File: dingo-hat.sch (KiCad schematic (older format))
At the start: 50 parts, among them J1 6-13V, J14 NEOPIXEL, J15 MPU-9250, J16 4, J17 5, J18 6, J19 7, J2 Raspberry_Pi_2_3, J24 3mm_Mount, J25 3mm_Mount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

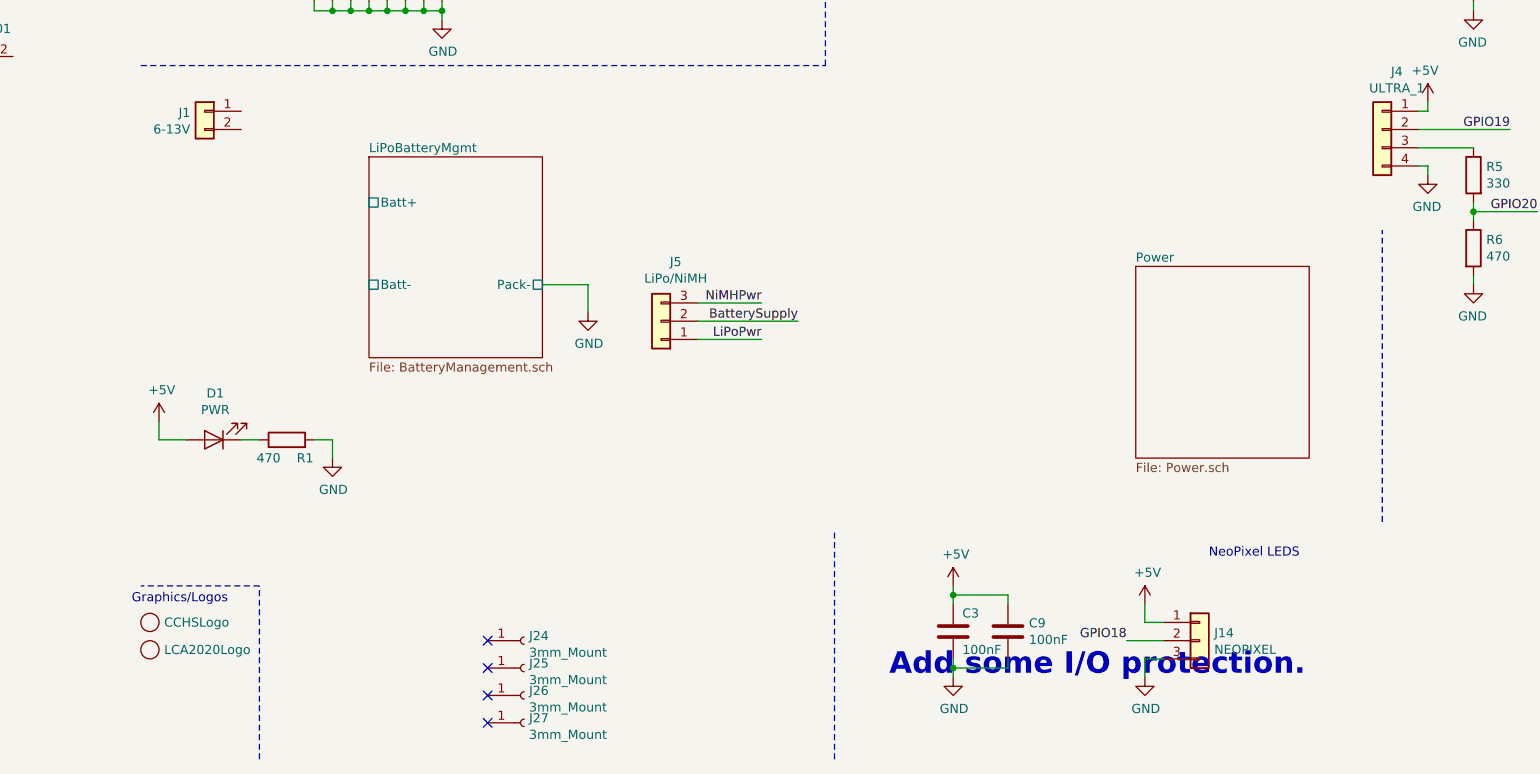
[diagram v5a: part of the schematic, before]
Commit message: Adding ADC for battery level.
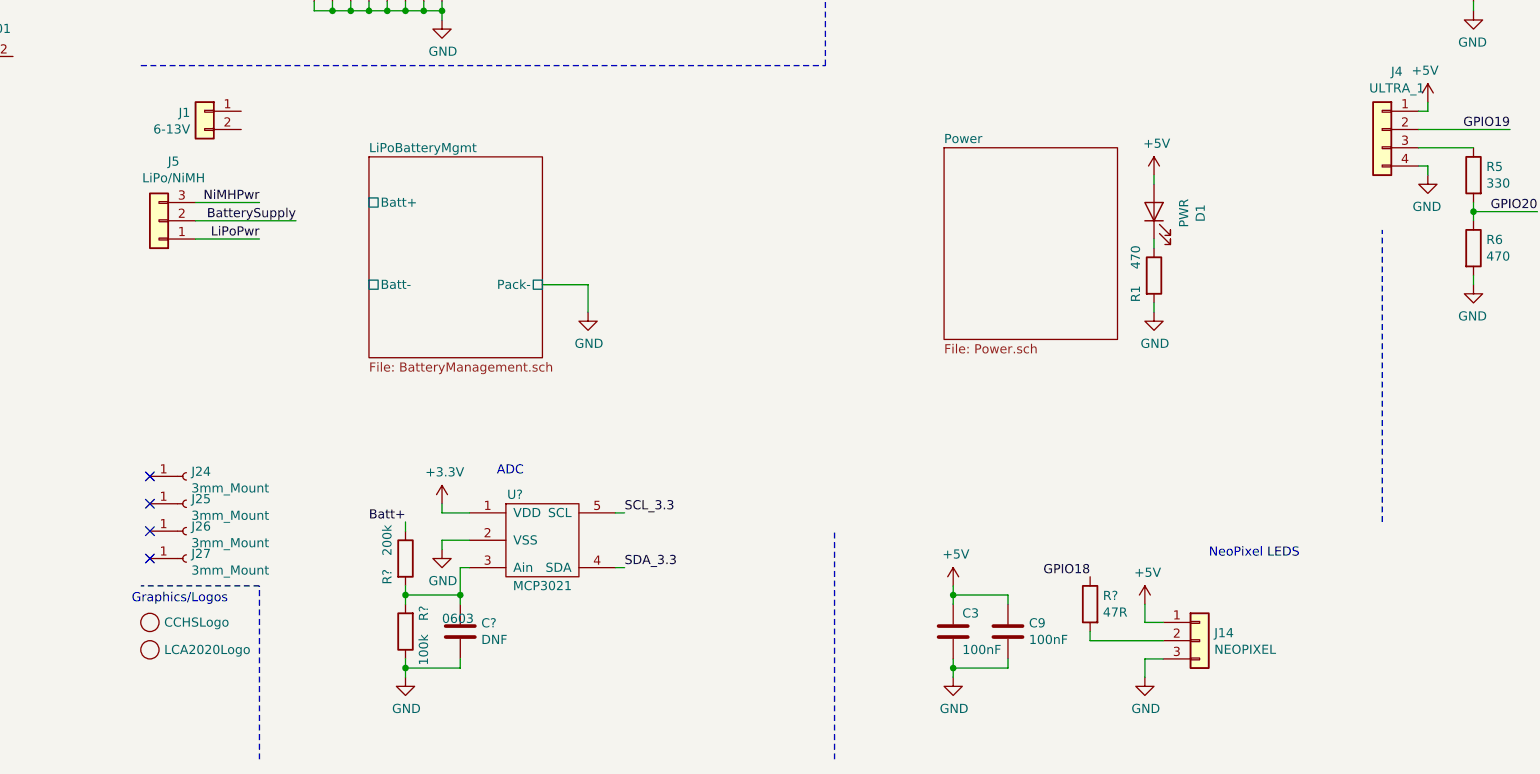
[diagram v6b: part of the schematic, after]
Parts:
- added C?: DNF, Capacitors_SMD:C_0603, symbol Device:C
- added R?: 100k, Resistors_SMD:R_0603, symbol Device:R
- added R?: 200k, Resistors_SMD:R_0603, symbol Device:R
- added R?: 47R, Resistors_SMD:R_0603, symbol Device:R
- added U?: MCP3021, TO_SOT_Packages_SMD:SOT-23-5, symbol dingo-hat:MCP3021
- R1, R3, R4, R5, R6, R7: footprint Resistor_SMD:R_0603_1608Metric_Pad1.05x0.95mm_HandSolder -> Resistors_SMD:R_0603
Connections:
- net +3V3: now also U?.1 (VDD)
- net GND: now also C?.2, R?.1, U?.2 (VSS)
- net GPIO18: now also R?.1; no longer J14.2 (Pin_2)
- net SCL_3.3: now also U?.5 (SCL)
- net SDA_3.3: now also U?.4 (SDA)
- new net: J14.2 (Pin_2), R?.2
- new net: C?.1, R?.2, R?.2, U?.3 (Ain)
- new net Batt+: R?.1
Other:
- note added: "ADC"
- note removed: "Add some I/O protection."
- moved on the sheet: D1, J24, J25, J26, J27, J5, R1

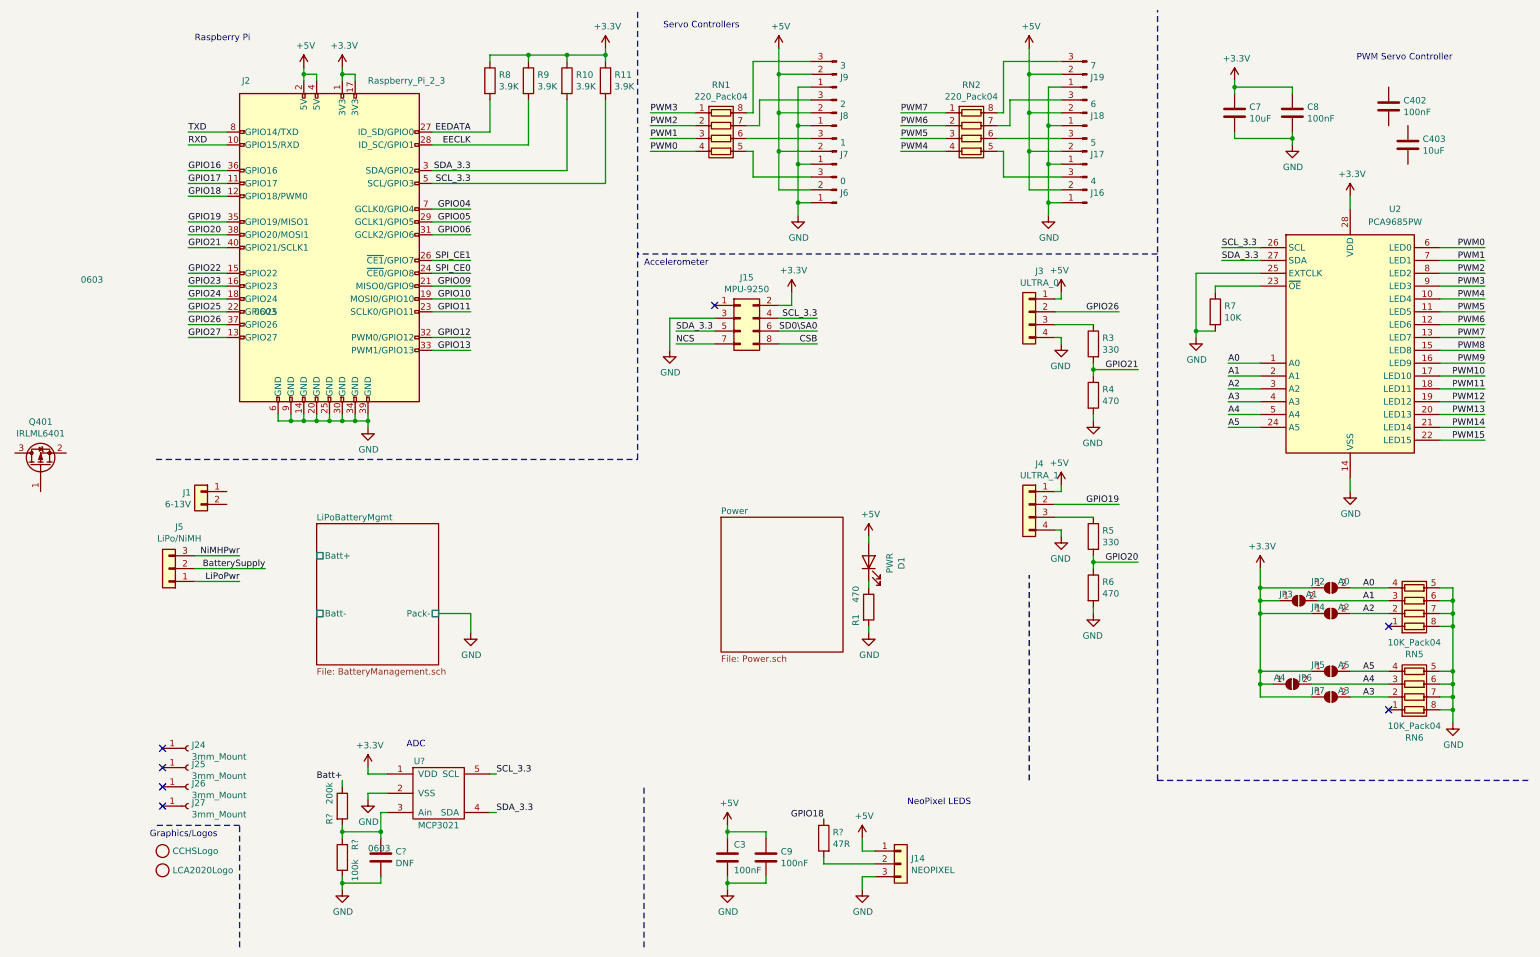
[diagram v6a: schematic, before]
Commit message: Getting rid of address block on PCA9685. We don't need that many options.
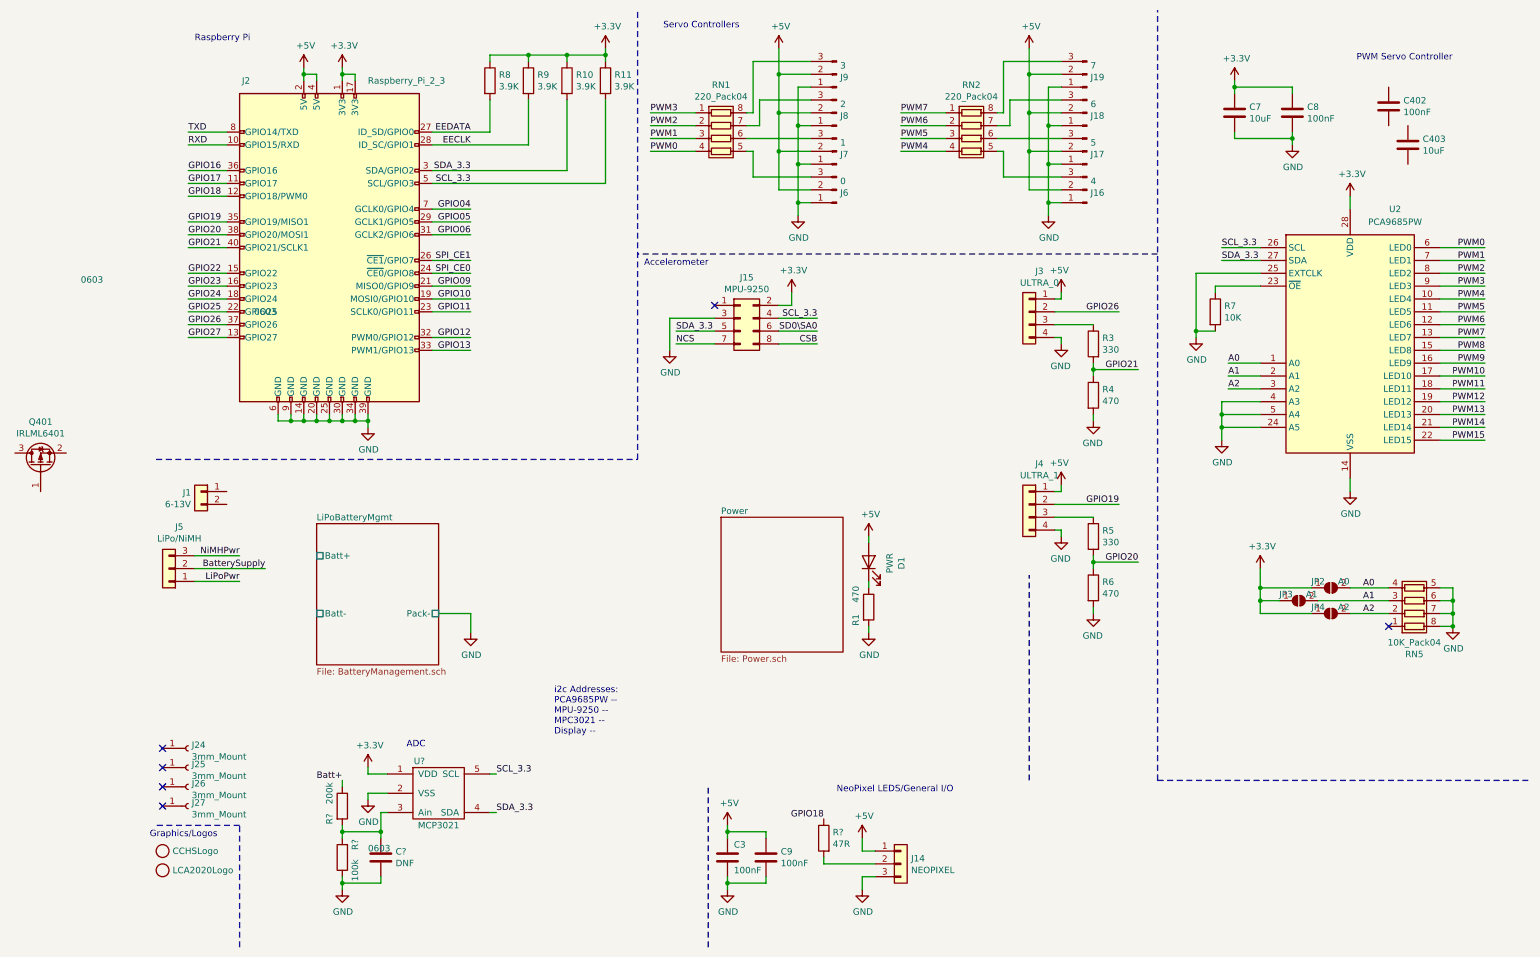
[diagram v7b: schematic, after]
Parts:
- removed JP5: A5, Jumper:SolderJumper-2_P1.3mm_Open_RoundedPad1.0x1.5mm, symbol Jumper:SolderJumper_2_Open
- removed JP6: A4, Jumper:SolderJumper-2_P1.3mm_Open_RoundedPad1.0x1.5mm, symbol Jumper:SolderJumper_2_Open
- removed JP7: A3, Jumper:SolderJumper-2_P1.3mm_Open_RoundedPad1.0x1.5mm, symbol Jumper:SolderJumper_2_Open
- removed RN6: 10K_Pack04, Resistor_SMD:R_Array_Convex_4x0603, symbol Device:R_Pack04
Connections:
- net A3 is gone; now on net GND: U2.4 (A3)
- net A4 is gone; now on net GND: U2.5 (A4)
- net A5 is gone; now on net GND: U2.24 (A5)
- no-connect marks 7 -> 6
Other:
- note added: "NeoPixel LEDS/General I/O"
- note added: "i2c Addresses:\nPCA9685PW --\nMPU-9250 --\nMPC3021 --\nDisplay --"
- note removed: "NeoPixel LEDS"
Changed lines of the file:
@@
 Text Label 8850 3450 0    50   ~ 0
 A2
-Wire Wire Line
-	9100 3550 8850 3550
-Text Label 8850 3550 0    50   ~ 0
-A3
-Wire Wire Line
-	9100 3650 8850 3650
-Text Label 8850 3650 0    50   ~ 0
-A4
-Wire Wire Line
-	9100 3750 8850 3750
-Text Label 8850 3750 0    50   ~ 0
-A5
 $Comp
 L Device:R R7
@@
 $EndComp
 $Comp
-L power:GND #PWR0107
-U 1 1 5C001B2D
-P 10600 6050
-F 0 "#PWR0107" H 10600 5800 50  0001 C CNN
-F 1 "GND" H 10605 5877 50  0000 C CNN
-F 2 "" H 10600 6050 50  0001 C CNN
-F 3 "" H 10600 6050 50  0001 C CNN
-	1    10600 6050
-	1    0    0    -1
-$EndComp
-$Comp
 L Jumper:SolderJumper_2_Open JP2
 U 1 1 5C001CDA
@@
 F 3 "~" H 9650 5200 50  0001 C CNN
 	1    9650 5200
-	1    0    0    -1
-$EndComp
-$Comp
-L Jumper:SolderJumper_2_Open JP5
-U 1 1 5C00261D
-P 9650 5650
-F 0 "JP5" H 9550 5700 50  0000 C CNN
-F 1 "A5" H 9750 5700 50  0000 C CNN
-F 2 "Jumper:SolderJumper-2_P1.3mm_Open_RoundedPad1.0x1.5mm" H 9650 5650 50  0001 C CNN
-F 3 "~" H 9650 5650 50  0001 C CNN
-	1    9650 5650
-	1    0    0    -1
-$EndComp
-$Comp
-L Jumper:SolderJumper_2_Open JP6
-U 1 1 5C002EE1
-P 9350 5750
-F 0 "JP6" H 9450 5800 50  0000 C CNN
-F 1 "A4" H 9250 5800 50  0000 C CNN
-F 2 "Jumper:SolderJumper-2_P1.3mm_Open_RoundedPad1.0x1.5mm" H 9350 5750 50  0001 C CNN
-F 3 "~" H 9350 5750 50  0001 C CNN
-	1    9350 5750
-	1    0    0    -1
-$EndComp
-$Comp
-L Jumper:SolderJumper_2_Open JP7
-U 1 1 5C002EE7
-P 9650 5850
-F 0 "JP7" H 9550 5900 50  0000 C CNN
-F 1 "A3" H 9750 5900 50  0000 C CNN
-F 2 "Jumper:SolderJumper-2_P1.3mm_Open_RoundedPad1.0x1.5mm" H 9650 5850 50  0001 C CNN
-F 3 "~" H 9650 5850 50  0001 C CNN
-	1    9650 5850
 	1    0    0    -1
 $EndComp
@@
 	6000 7250 6000 7350
 Wire Notes Line
-	4300 7800 4300 6550
-Text Notes 6350 6700 0    50   ~ 0
-NeoPixel LEDS
+	4800 7800 4800 6550
+Text Notes 5800 6600 0    50   ~ 0
+NeoPixel LEDS/General I/O
 Wire Notes Line
 	8300 2400 4250 2400
@@
 NoConn ~ 550  6700
 $Comp
-L Device:R_Pack04 RN6
-U 1 1 5C46C610
-P 10300 5750
-F 0 "RN6" V 9883 5750 50  0000 C CNN
-F 1 "10K_Pack04" V 9974 5750 50  0000 C CNN
-F 2 "Resistor_SMD:R_Array_Convex_4x0603" V 10575 5750 50  0001 C CNN
-F 3 "~" H 10300 5750 50  0001 C CNN
-F 4 "SMD" H 0   0   50  0001 C CNN "Package"
-	1    10300 5750
-	0    1    -1   0
-$EndComp
-$Comp
 L Device:R_Pack04 RN5
 U 1 1 5C4B78BC
@@
 	9100 4850 9100 5000
 Wire Wire Line
-	9100 5850 9500 5850
-Wire Wire Line
-	9200 5750 9100 5750
-Connection ~ 9100 5750
-Wire Wire Line
-	9100 5750 9100 5850
-Wire Wire Line
-	9500 5650 9100 5650
-Connection ~ 9100 5650
-Wire Wire Line
-	9100 5650 9100 5750
-Wire Wire Line
 	9100 5000 9500 5000
 Connection ~ 9100 5000
@@
 Wire Wire Line
 	9500 5200 9100 5200
-Connection ~ 9100 5200
-Wire Wire Line
-	9100 5200 9100 5650
-Wire Wire Line
-	9800 5650 10100 5650
-Wire Wire Line
-	9500 5750 10100 5750
-Wire Wire Line
-	9800 5850 10100 5850
 Wire Wire Line
 	10500 5000 10600 5000
@@
 	10600 5000 10600 5100
 Wire Wire Line
-	10500 5950 10600 5950
-Connection ~ 10600 5950
-Wire Wire Line
-	10600 5950 10600 6050
-Wire Wire Line
-	10600 5850 10500 5850
-Connection ~ 10600 5850
-Wire Wire Line
-	10600 5850 10600 5950
-Wire Wire Line
-	10500 5750 10600 5750
-Connection ~ 10600 5750
-Wire Wire Line
-	10600 5750 10600 5850
-Wire Wire Line
-	10500 5650 10600 5650
-Connection ~ 10600 5650
-Wire Wire Line
-	10600 5650 10600 5750
-Wire Wire Line
 	10500 5300 10600 5300
-Connection ~ 10600 5300
-Wire Wire Line
-	10600 5300 10600 5650
 Wire Wire Line
 	10500 5200 10600 5200
@@
 	9800 5200 10100 5200
 NoConn ~ 10100 5300
-NoConn ~ 10100 5950
 Text Label 9900 5000 0    50   ~ 0
 A0
@@
 Text Label 9900 5200 0    50   ~ 0
 A2
-Text Label 9900 5850 0    50   ~ 0
-A3
-Text Label 9900 5750 0    50   ~ 0
-A4
-Text Label 9900 5650 0    50   ~ 0
-A5
 $Comp
 L Device:C C9
@@
 Text Notes 2450 6250 0    50   ~ 0
 ADC
+Text Notes 3600 6150 0    50   ~ 0
+i2c Addresses:\nPCA9685PW --\nMPU-9250 --\nMPC3021 --\nDisplay --
+$Comp
+L power:GND #PWR?
+U 1 1 5E262FFC
+P 10600 5300
+F 0 "#PWR?" H 10600 5050 50  0001 C CNN
+F 1 "GND" H 10605 5127 50  0000 C CNN
+F 2 "" H 10600 5300 50  0001 C CNN
+F 3 "" H 10600 5300 50  0001 C CNN
+	1    10600 5300
+	1    0    0    -1
+$EndComp
+Connection ~ 10600 5300
+$Comp
+L power:GND #PWR?
+U 1 1 5E2ACCA1
+P 8800 3850
+F 0 "#PWR?" H 8800 3600 50  0001 C CNN
+F 1 "GND" H 8805 3677 50  0000 C CNN
+F 2 "" H 8800 3850 50  0001 C CNN
+F 3 "" H 8800 3850 50  0001 C CNN
+	1    8800 3850
+	1    0    0    -1
+$EndComp
+Wire Wire Line
+	8800 3750 8800 3850
+Wire Wire Line
+	8800 3750 9100 3750
+Wire Wire Line
+	8800 3750 8800 3650
+Wire Wire Line
+	8800 3550 9100 3550
+Connection ~ 8800 3750
+Wire Wire Line
+	8800 3650 9100 3650
+Connection ~ 8800 3650
+Wire Wire Line
+	8800 3650 8800 3550
 $EndSCHEMATC
